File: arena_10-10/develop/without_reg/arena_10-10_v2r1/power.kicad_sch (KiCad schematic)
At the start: 6 parts, among them J25 Barrel_Jack, J26 XT30 Female, SW1 SW_SPDT, U110 NID100-5, U82 RB-XXYYD

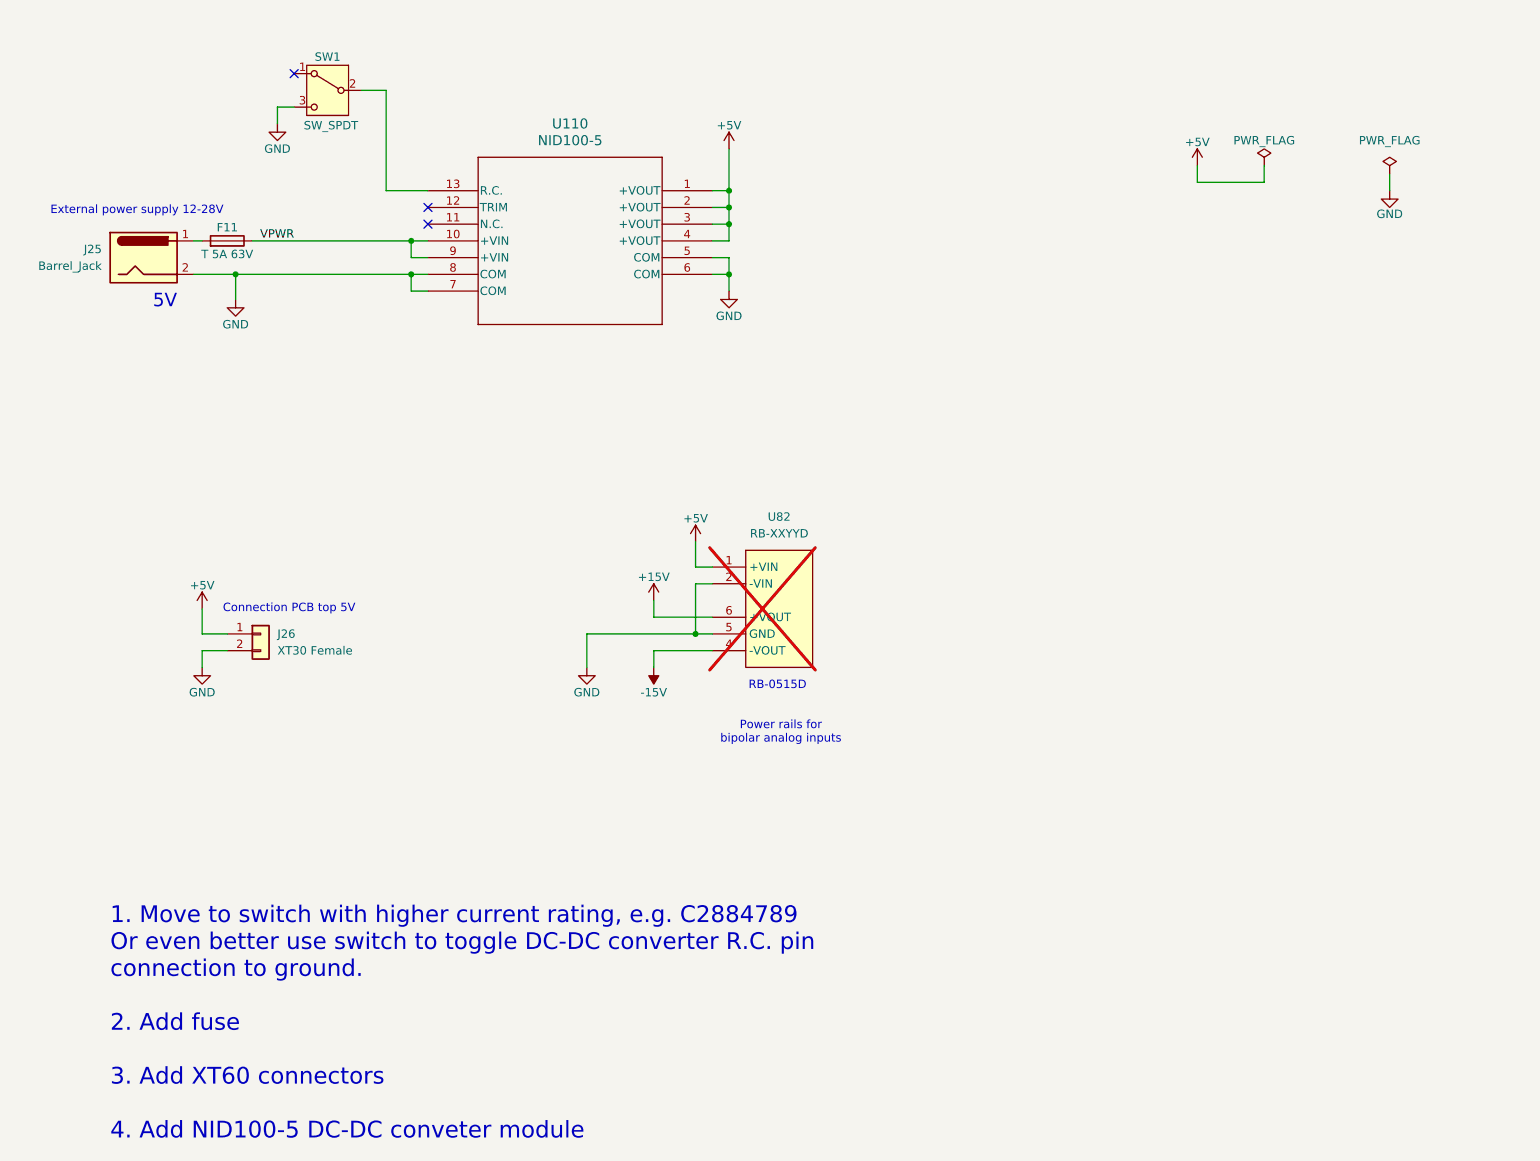
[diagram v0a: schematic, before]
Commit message: Finished preliminary layout for efuse design.
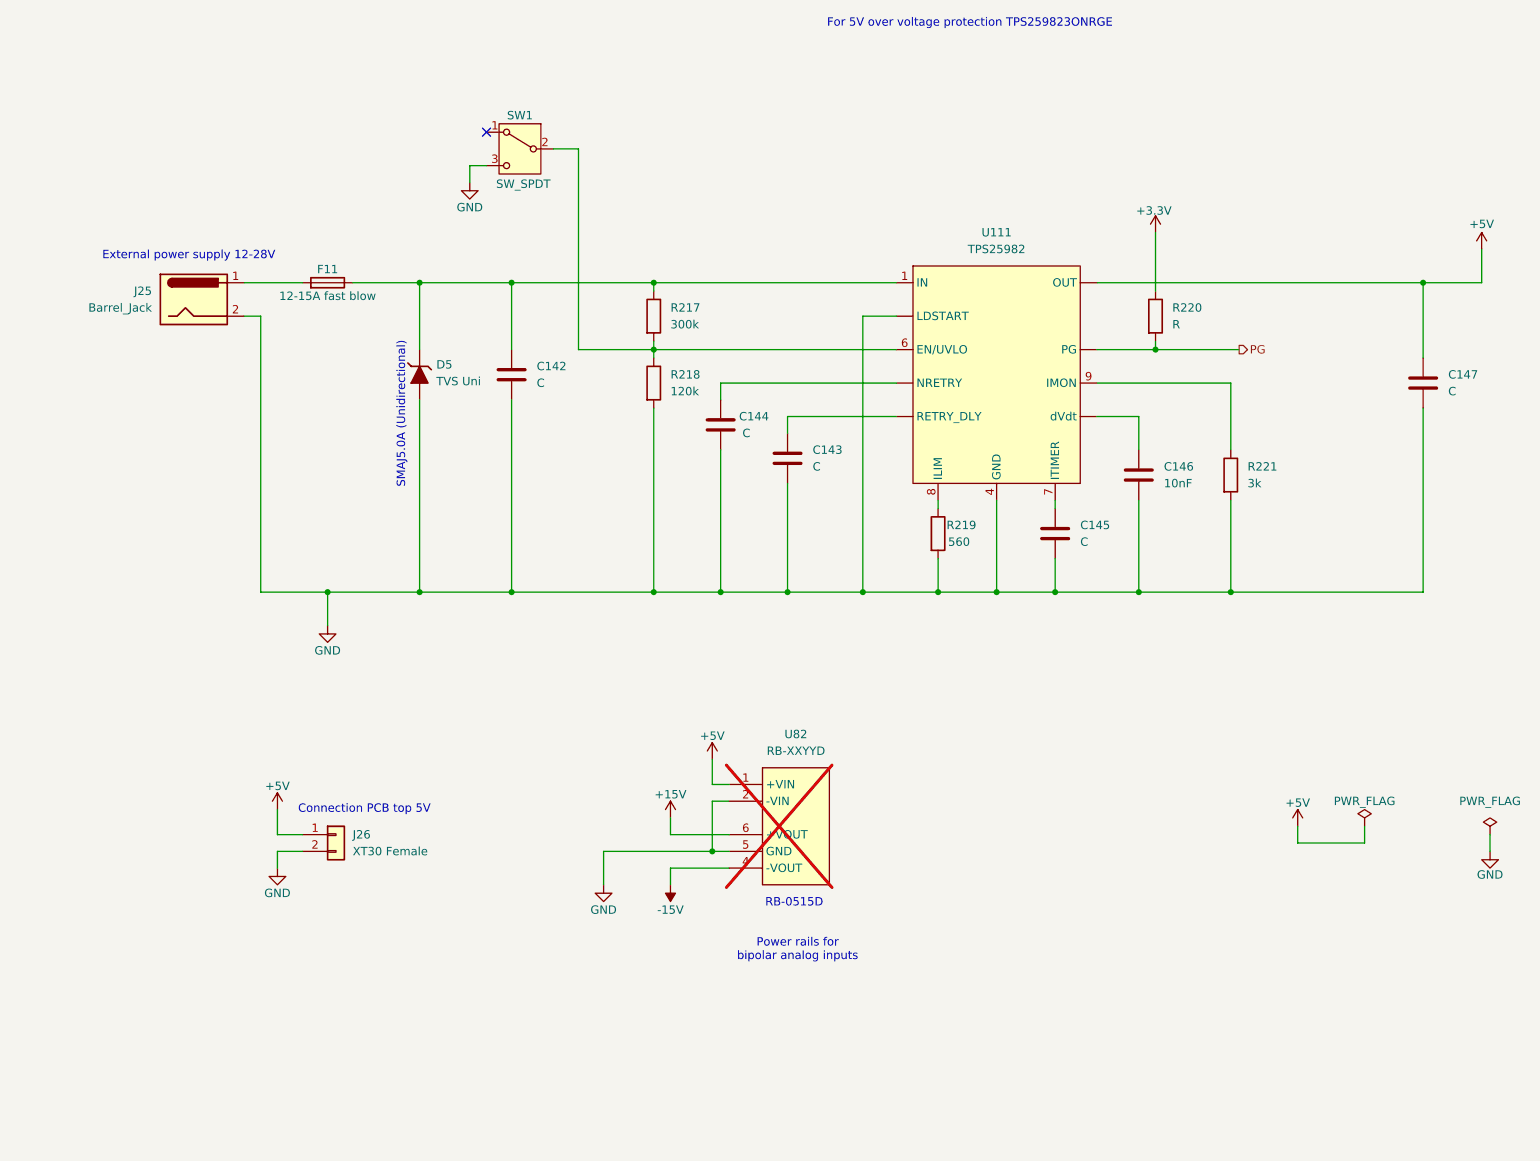
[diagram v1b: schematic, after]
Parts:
- removed U110: NID100-5, NID100-5:NID100_MWU, symbol NID100-5:NID100-5
- added C142, C143, C144, C145, C147: C, symbol Device:C
- added C146: 10nF, symbol Device:C
- added D5: TVS Uni, symbol TVS_Unidirectional:TVS_Uni
- added R217: 300k, symbol Device:R
- added R218: 120k, symbol Device:R
- added R219: 560, symbol Device:R
- added R220: R, symbol Device:R
- added R221: 3k, symbol Device:R
- added U111: TPS25982, Package_SON:VSON-10-1EP_3x3mm_P0.5mm_EP1.65x2.4mm_ThermalVias, symbol TPS25982:TPS25982
- F11: value T 5A 63V -> 12-15A fast blow
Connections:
- net +5V: now also C147.1, U111. (dVdt)
- net GND: now also C142.2, C143.2, C144.2, C145.2, C146.2, C147.2, D5.2 (A), R218.2, R219.2, R221.2, U111. (dVdt), U111.26 (GND), U111.4 (GND), U111.5 (GND)
- net at SW1.2 (B): now also R217.2, R218.1, U111.6 (EN/UVLO)
- net VPWR renamed IN
- net IN: now also C142.1, D5.1 (K), R217.1, U111.1 (IN), U111.2 (IN), U111.25 (IN), U111.3 (IN)
- new net: R221.1, U111.9 (IMON)
- new net: C143.1, U111. (dVdt)
- new net: C144.1, U111. (dVdt)
- new net: C146.1, U111. (dVdt)
- new net: C145.1, U111.7 (ITIMER)
- new net: R219.1, U111.8 (ILIM)
- new net +3.3V: R220.1
- new net PG: R220.2, U111. (dVdt)
- no-connect marks 3 -> 1
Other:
- note added: "For 5V over voltage protection TPS259823ONRGE"
- note added: "SMAJ5.0A (Unidirectional)"
- note removed: "1. Move to switch with higher current rating, e.g. C2884789 Or even better use switch to toggle DC-DC converter R.C. pin connection to ground. 2. Add fuse 3. Add XT60 connectors 4. Add NID100-5 DC-DC conveter module"
- note removed: "5V"
- moved on the sheet: F11, J25, J26, SW1, U82

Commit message: Worked more on layout for 10 10 arena with efuse.
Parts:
- added C148: 100nF, Capacitor_SMD:C_0402_1005Metric, symbol Device:C
- added C149: 0.1uF,25V min, Capacitor_SMD:C_0402_1005Metric, symbol Device:C
- added C150, C151: 10nF, Capacitor_SMD:C_0402_1005Metric, symbol Device:C
- added D6: B340A, Diode_SMD:D_SMA, symbol Device:D_Schottky_Filled
- added R222, R225: 10k, Resistor_SMD:R_0402_1005Metric, symbol Device:R
- added R223: 133k, Resistor_SMD:R_0402_1005Metric, symbol Device:R
- added R224: 100, Resistor_SMD:R_0402_1005Metric, symbol Device:R
- added U110: TLV6700, Package_TO_SOT_SMD:SOT-23-6, symbol TLV6700:TLV6700
- C142: value C -> 0.1uF, >=25V; footprint (none) -> Capacitor_SMD:C_0402_1005Metric
- C143: value C -> 10nF; footprint (none) -> Capacitor_SMD:C_0402_1005Metric
- C144: value C -> 22nF; footprint (none) -> Capacitor_SMD:C_0402_1005Metric
- C145: value C -> 2.2nF,C0G; footprint (none) -> Capacitor_SMD:C_0402_1005Metric
- C146: value 10nF -> 10nF, C0G, >=25V; footprint (none) -> Capacitor_SMD:C_0402_1005Metric
- C147: value C -> 10uF; footprint (none) -> Capacitor_SMD:C_1206_3216Metric
- D5: value TVS Uni -> SMAJ13A; footprint (none) -> Diode_SMD:D_SMA
- F11: footprint Fuse:Fuse_1206_3216Metric -> Fuse:Fuse_Littelfuse-NANO2-451_453; LCSC Part # C1972666 -> C99549
- R217: value 300k -> 100k; footprint (none) -> Resistor_SMD:R_0402_1005Metric
- R218: value 120k -> 36.5k; footprint (none) -> Resistor_SMD:R_0402_1005Metric
- R219: value 560 -> 182; footprint (none) -> Resistor_SMD:R_0402_1005Metric
- R220: value R -> 10k; footprint (none) -> Resistor_SMD:R_0402_1005Metric; LCSC Part # (none) -> C190095
- R221: value 3k -> 1.33k; footprint (none) -> Resistor_SMD:R_0402_1005Metric
- U111: footprint Package_SON:VSON-10-1EP_3x3mm_P0.5mm_EP1.65x2.4mm_ThermalVias -> TPS25982:QFN_59823ONRGER
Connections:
- net +5V: now also U111.17 (OUT), U111.18 (OUT), U111.19 (OUT), U111.20 (OUT), U111.21 (OUT), U111.22 (OUT), U111.23 (OUT), U111.24 (OUT), D6.1 (K); no longer U111. (dVdt)
- net GND: now also U111.12 (LDSTART), U111.14 (GND), U111.25 (GND), C148.2, C149.2, C150.2, C151.2, D6.2 (A), R225.1, U110.2 (GND), U110.3 (INA+); no longer U111. (dVdt), U111.26 (GND)
- net IN: now also U111.16 (IN), U111.26 (IN), R223.2, R224.2; no longer U111.25 (IN)
- net PG: now also U111.13 (PG); no longer U111. (dVdt)
- net VIN_JACK: now reaches F11.2, J25.1
- net at R217.2, R218.1, SW1.2 (B)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: now also C150.1, U110.6 (OUTB)
- net at R221.1, U111.9 (IMON): now also R222.1
- net at C143.1: now also U111.10 (RETRY_DLY); no longer U111. (dVdt)
- net at C144.1: now also U111.11 (NRETRY); no longer U111. (dVdt)
- net at C146.1: now also U111.15 (dVdt); no longer U111. (dVdt)
- new net: C149.1, R224.1, U110.5 (VDD)
- new net: C151.1, R223.1, R225.2, U110.4 (INB-)
- new net IMON: C148.1, R222.2
- no-connect marks 1 -> 2
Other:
- note added: "EFuse"
- note added: "External Power 5V, 10A"
- note added: "IC Variant ---------- TPS259823ONRGE has over voltage lockout threshold = 7.6V w/ circuit breaker this combination provides over voltage protection for > 7.6V (if TLV6700 fails) Under voltage protection ---------------------------- R_VL1 and R_VL2 form a divider from IN to the EN/UVLO pin. It sets the input voltage below which the eFuse keeps its output off The EN/UVLO pin has a comparator with a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"
- note added: "Notes on TPS25982 efuse setup"
- note added: "Power Switch"
- note added: "Trip Current ------------ R_ILIM = 1460/(I_ILIM - 0.11), Select trip current to about 8A. This is below supply's 10A (10.5A trip) Ensures efuse trips first Choose I_ILIM = 8A => R_ILIM = 1460/(8 - 0.11) = 185 Ohms. Closest E96 value <= is 182 Ohms this gives I_ILIM = 8.13A w/ R_ILIM = 182 Ohms Inrush and startup ------------------ SR (V/ms) = I_INRUSH / C_OUT (uF) C_dVdt (pF) = 4600 / SR (V/ms) C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"
- note added: "current monitor (0-3V)"
- note added: "over voltage protection"
- note added: "power good (0 or 3.3V)"
- note removed: "External power supply 12-28V"
- note removed: "For 5V over voltage protection TPS259823ONRGE"
- note removed: "SMAJ5.0A (Unidirectional)"
- moved on the sheet: C142, C143, C144, C145, C146, C147, D5, F11, J25, J26, R217, R218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
